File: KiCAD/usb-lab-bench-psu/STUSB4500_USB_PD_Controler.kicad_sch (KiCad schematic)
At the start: 26 parts, among them J21 Conn_02x03_Top_Bottom, Q1 PMOS, Q2 PMOS, SW10 SW_Push, U13 STUSB4500QTR

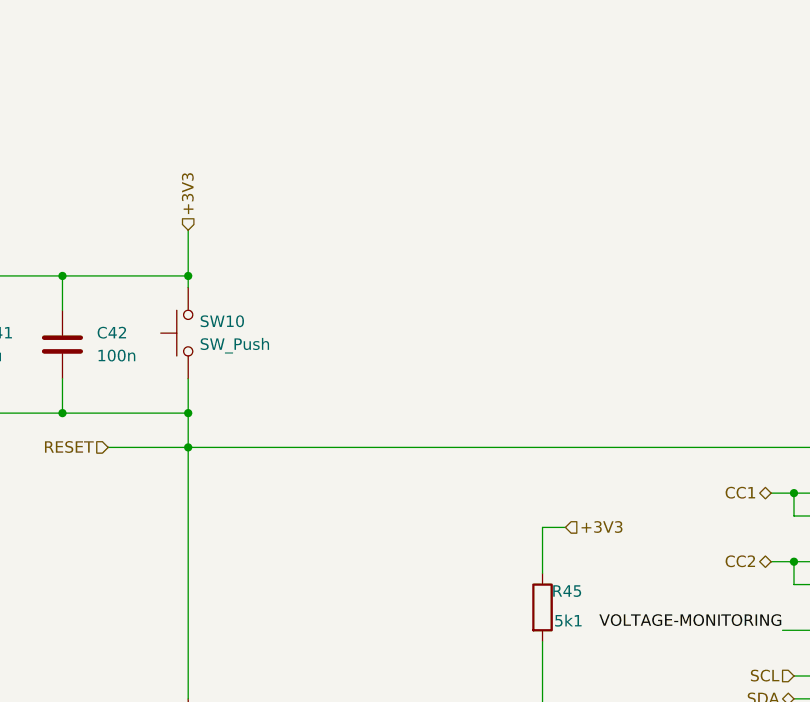
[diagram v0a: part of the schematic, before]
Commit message: Fixed label directions
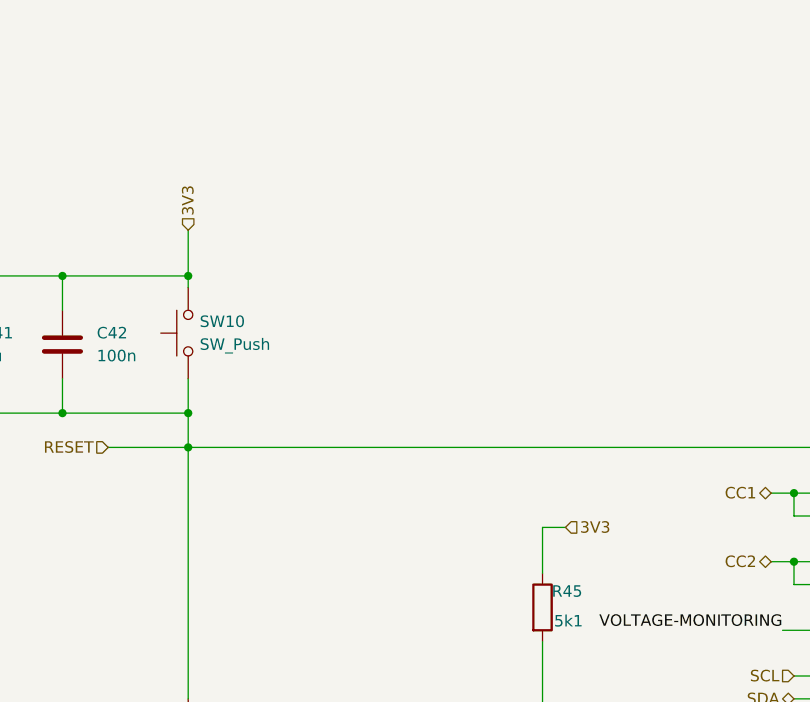
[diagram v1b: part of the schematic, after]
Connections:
- net +3V3 renamed 3V3
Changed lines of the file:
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@@
 		)
 	)
-	(hierarchical_label "+3V3"
+	(hierarchical_label "3V3"
 		(shape input)
 		(at 100.33 138.43 0)
@@
 		)
 	)
-	(hierarchical_label "+3V3"
+	(hierarchical_label "3V3"
 		(shape input)
 		(at 58.42 105.41 90)

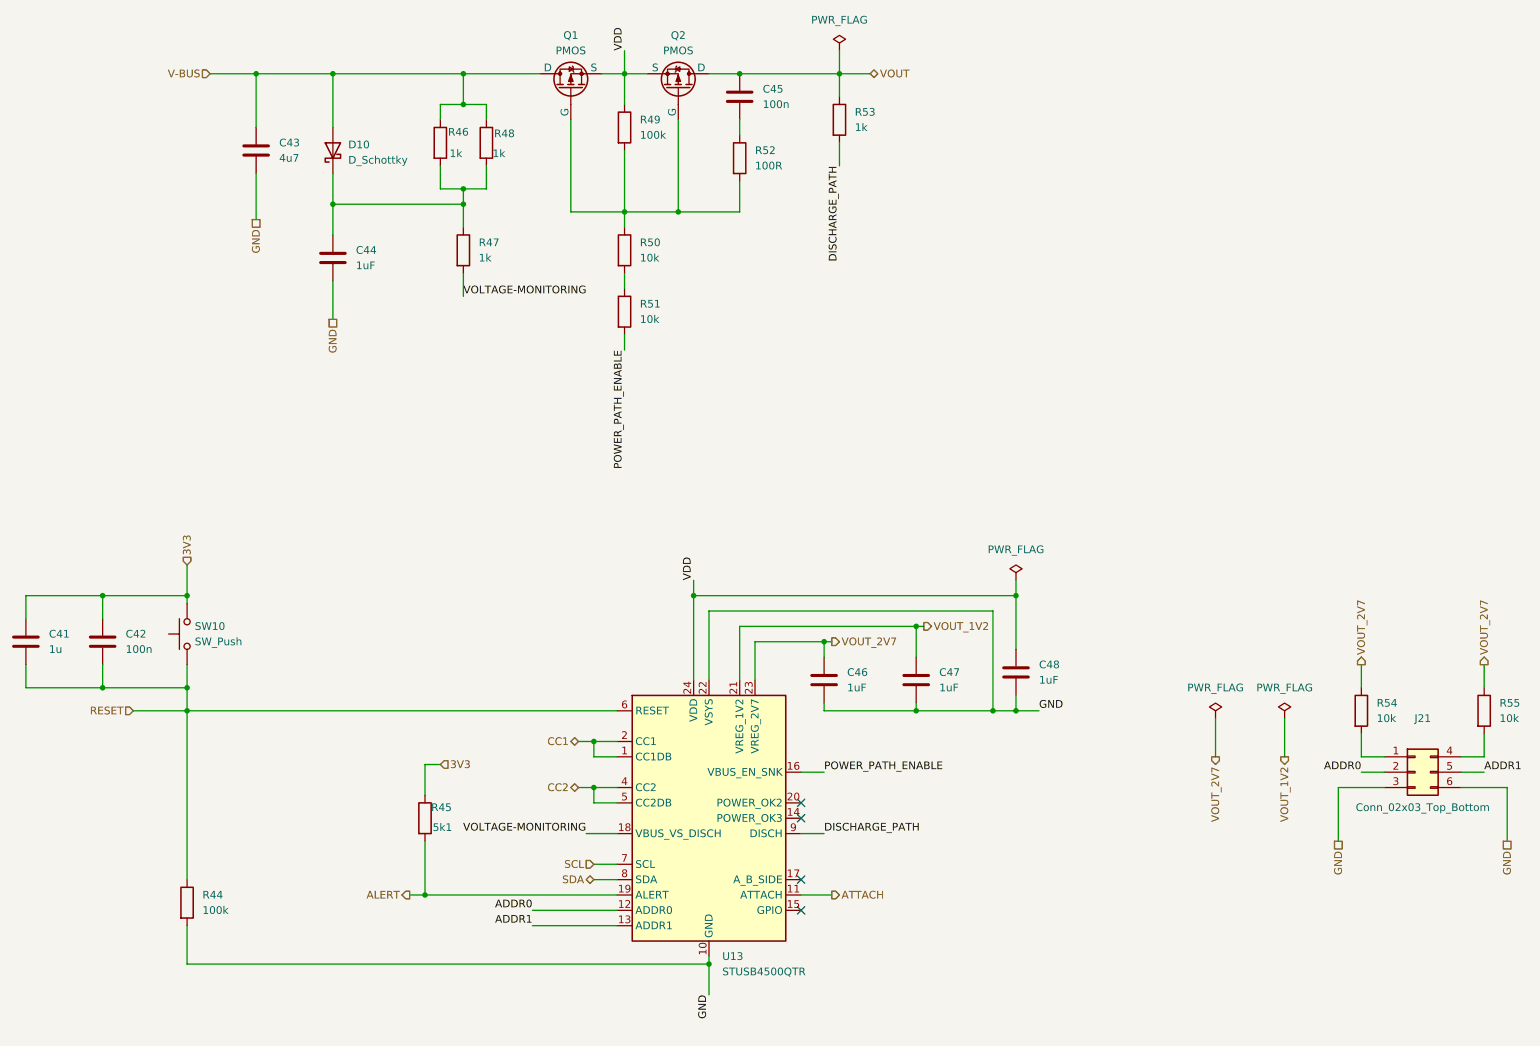
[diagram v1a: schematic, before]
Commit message: tweaked design of current limiter, added GPIO expander to USB-PD circuit
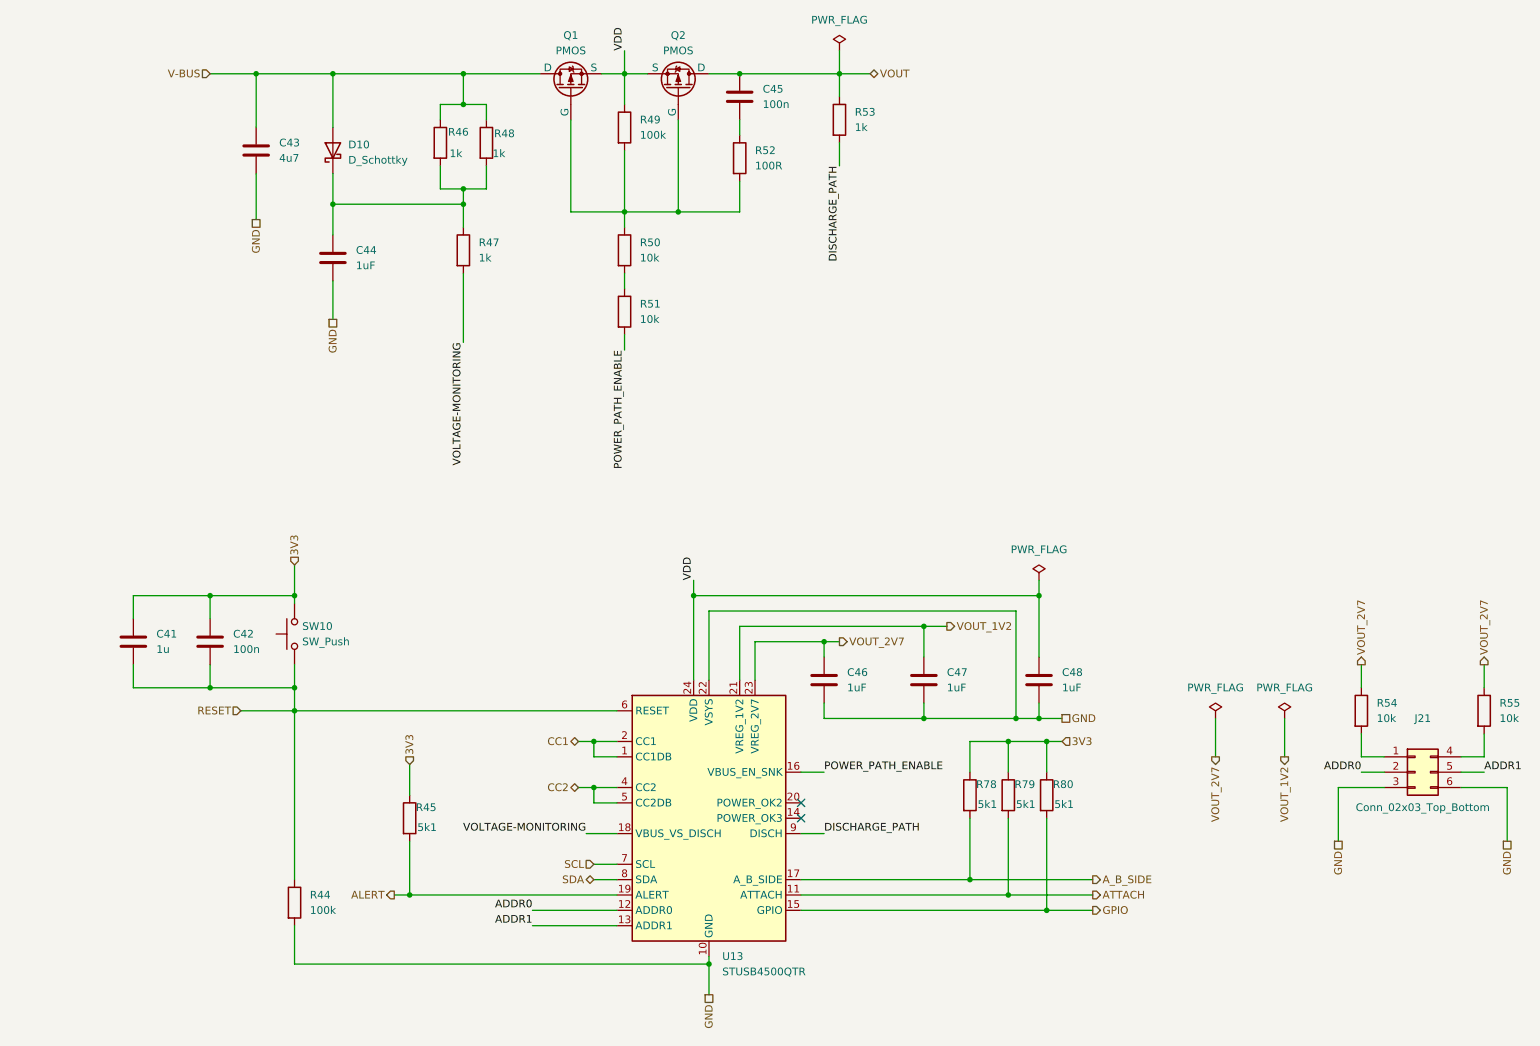
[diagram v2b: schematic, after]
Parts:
- added R78, R79, R80: 5k1, symbol Device:R
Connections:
- net 3V3: now also R78.1, R79.1, R80.1
- net ATTACH: now also R79.2
- net GPIO: now reaches U13.15 (GPIO)
- net GPIO: now also R80.2
- net A_B_SIDE: now reaches U13.17 (A_B_SIDE)
- net A_B_SIDE: now also R78.2
- no-connect marks 4 -> 2
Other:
- moved on the sheet: C41, C42, C47, C48, R44, R45, SW10
